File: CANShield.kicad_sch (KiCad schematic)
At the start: 1 part, among them U1 NUCLEO64-F411RE

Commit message: Save schematics
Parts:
- removed U1: NUCLEO64-F411RE, Module:ST_Morpho_Connector_144_STLink, symbol MCU_Module:NUCLEO64-F411RE
- added C1, C2, C3, C4, C5, C6: C, symbol Device:C
- added D1: ESDA5V3L, Package_TO_SOT_SMD:SOT-23-3, symbol Power_Protection:ESDA5V3L
- added FL1: Filter_EMI_LL_1423, symbol Device:Filter_EMI_LL_1423
- added J1, J2: Conn_02x19_Odd_Even, symbol Connector_Generic:Conn_02x19_Odd_Even
- added J3: Conn_01x06_Socket, symbol Connector:Conn_01x06_Socket
- added JP1: SolderJumper_2_Open, symbol Jumper:SolderJumper_2_Open
- added L1, L2, L3, L4: L_Ferrite, symbol Device:L_Ferrite
- added R1, R2, R3: R, symbol Device:R
- added U1: MCP2561-H-MF, Package_DFN_QFN:DFN-8-1EP_3x3mm_P0.65mm_EP1.55x2.4mm, symbol Interface_CAN_LIN:MCP2561-H-MF
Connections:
- new net: J3.3 (Pin_3), L3.1
- new net: C3.1, D1.2 (K), FL1.1, L3.2
- new net: C2.2, R1.2, R2.1, R3.2
- new net: JP1.1 (A), U1.5 (SPLIT)
- new net: JP1.2 (B), R3.1
- new net: C3.2, D1.1 (K), FL1.2, L4.2
- new net: J3.2 (Pin_2), J3.6 (Pin_6), L2.1
- new net: J3.1 (Pin_1), J3.5 (Pin_5), L1.1
- new net: J3.4 (Pin_4), L4.1
- new net +5V: C1.1, U1.3 (VDD)
- new net CAN_H: C4.2, C5.1, FL1.4, R1.1, U1.7 (CANH)
- new net CAN_L: C4.1, C6.2, FL1.3, R2.2, U1.6 (CANL)
- new net CAN_RXD: U1.4 (RXD)
- new net CAN_STBY: U1.8 (STBY)
- new net CAN_TXD: U1.1 (TXD)
- new net GND: C1.2, C2.1, C5.2, C6.1, D1.3 (A), J1.19 (Pin_19), J1.8 (Pin_8), J2.20 (Pin_20), L1.2, U1.2 (VSS), U1.9 (VSS)
- new net VBUS: L2.2

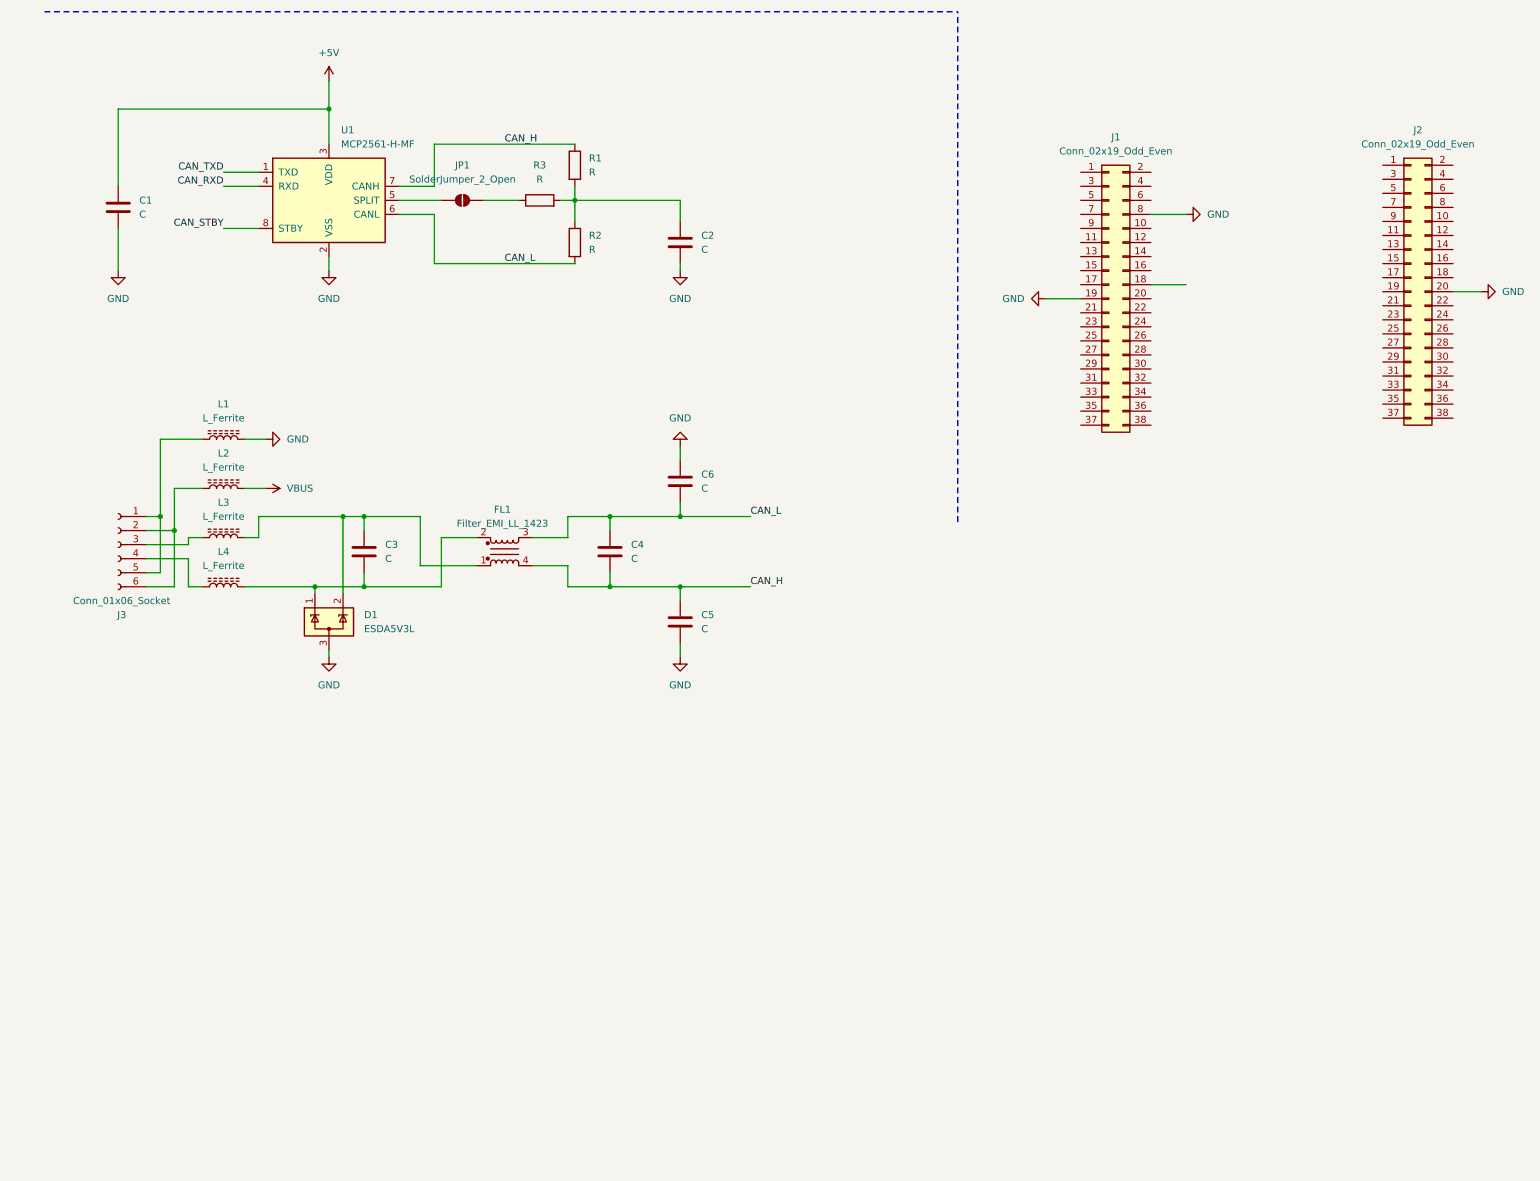
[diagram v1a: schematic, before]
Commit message: Add NXP TJA1443 CAN-FD Chip
Add reference design for CAN-FD chip
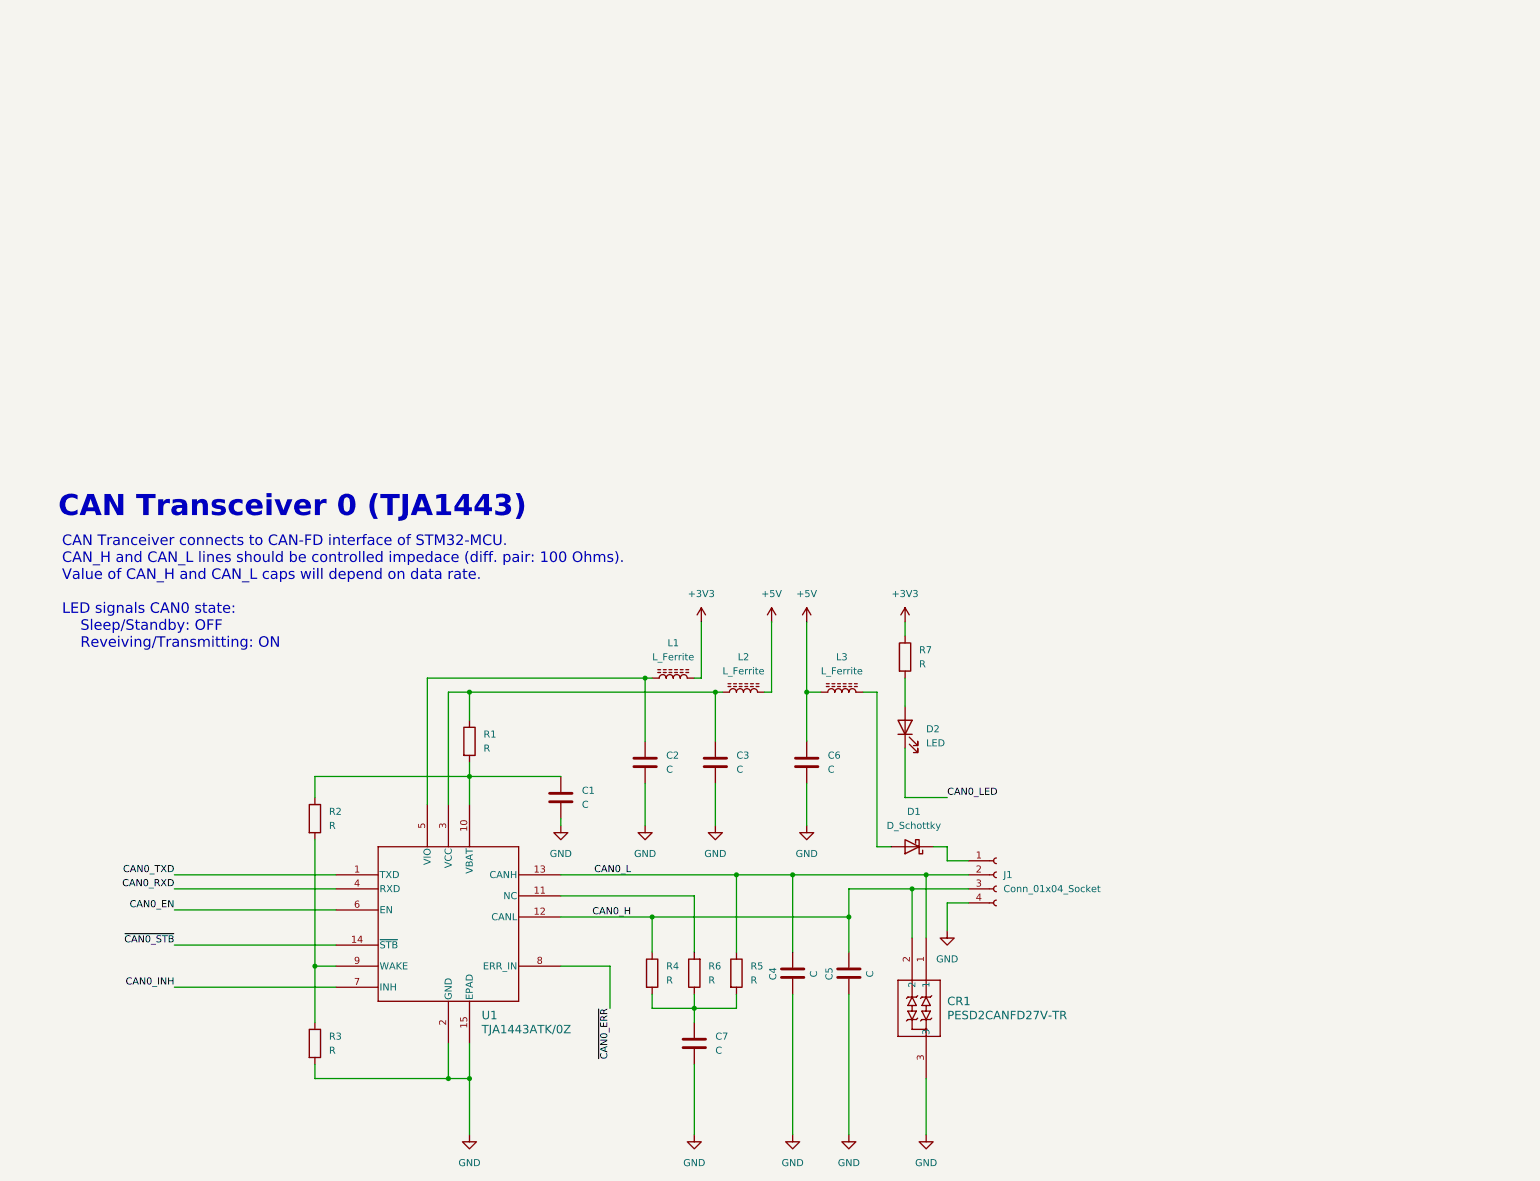
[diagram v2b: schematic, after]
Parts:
- removed D1: ESDA5V3L, Package_TO_SOT_SMD:SOT-23-3, symbol Power_Protection:ESDA5V3L
- removed FL1: Filter_EMI_LL_1423, symbol Device:Filter_EMI_LL_1423
- removed J1, J2: Conn_02x19_Odd_Even, symbol Connector_Generic:Conn_02x19_Odd_Even
- removed J3: Conn_01x06_Socket, symbol Connector:Conn_01x06_Socket
- removed JP1: SolderJumper_2_Open, symbol Jumper:SolderJumper_2_Open
- removed L4: L_Ferrite, symbol Device:L_Ferrite
- removed U1: MCP2561-H-MF, Package_DFN_QFN:DFN-8-1EP_3x3mm_P0.65mm_EP1.55x2.4mm, symbol Interface_CAN_LIN:MCP2561-H-MF
- added C7: C, symbol Device:C
- added CR1: PESD2CANFD27V-TR, SOT23_PESD2_NEX, symbol PESD2CANFD27V:PESD2CANFD27V-TR
- added D1: D_Schottky, symbol Device:D_Schottky
- added D2: LED, symbol Device:LED
- added J1: Conn_01x04_Socket, symbol Connector:Conn_01x04_Socket
- added R4, R5, R6, R7: R, symbol Device:R
- added U1: TJA1443ATK/0Z, HVSON14_SOT1086-2_NXP, symbol TJA1443ATK:TJA1443ATK_0Z
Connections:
- net VBUS is gone; now on net +5V: L2.2
- net +5V: now also C6.1, L3.1; no longer C1.1
- net GND: now also C2.2, C3.2, C4.2, C6.2, R3.2, C7.2, CR1.3, J1.4 (Pin_4), U1.15 (EPAD), U1.2 (GND); no longer C2.1, C6.1, L1.2
- net at C3.1: now also L2.1, R1.1, U1.3 (VCC); no longer L3.2
- net at R1.2, R2.1: now also C1.1, U1.10 (VBAT); no longer C2.2, R3.2
- net at R3.1: now also R2.2, U1.9 (WAKE)
- net at L1.1: now also C2.1, U1.5 (VIO)
- removed net CAN_H: C4.2, C5.1, R1.1
- removed net CAN_L: C4.1, C6.2, R2.2
- new net: R6.2, U1.11 (NC)
- new net: D1.1 (K), J1.1 (Pin_1)
- new net: D1.2 (A), L3.2
- new net: C7.1, R4.2, R5.2, R6.1
- new net: D2.2 (A), R7.2
- new net +3V3: L1.2, R7.1
- new net CAN0_EN: U1.6 (EN)
- new net CAN0_H: C5.1, CR1.2, J1.3 (Pin_3), R4.1, U1.12 (CANL)
- new net CAN0_INH: U1.7 (INH)
- new net CAN0_L: C4.1, CR1.1, J1.2 (Pin_2), R5.1, U1.13 (CANH)
- new net CAN0_LED: D2.1 (K)
- new net CAN0_RXD: U1.4 (RXD)
- new net CAN0_TXD: U1.1 (TXD)
- new net ~{CAN0_ERR}: U1.8 (ERR_IN)
- new net ~{CAN0_STB}: U1.14 (~{STB})
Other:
- note added: "CAN Tranceiver connects to CAN-FD interface of STM32-MCU. CAN_H and CAN_L lines should be controlled impedace (diff. pair: 100 Ohms). Value of CAN_H and CAN_L caps will depend on data rate. LED signals CAN0 state: Sleep/Standby: OFF Reveiving/Transmitting: ON"
- note added: "CAN Transceiver 0 (TJA1443)"
- title: (none) -> CANShield

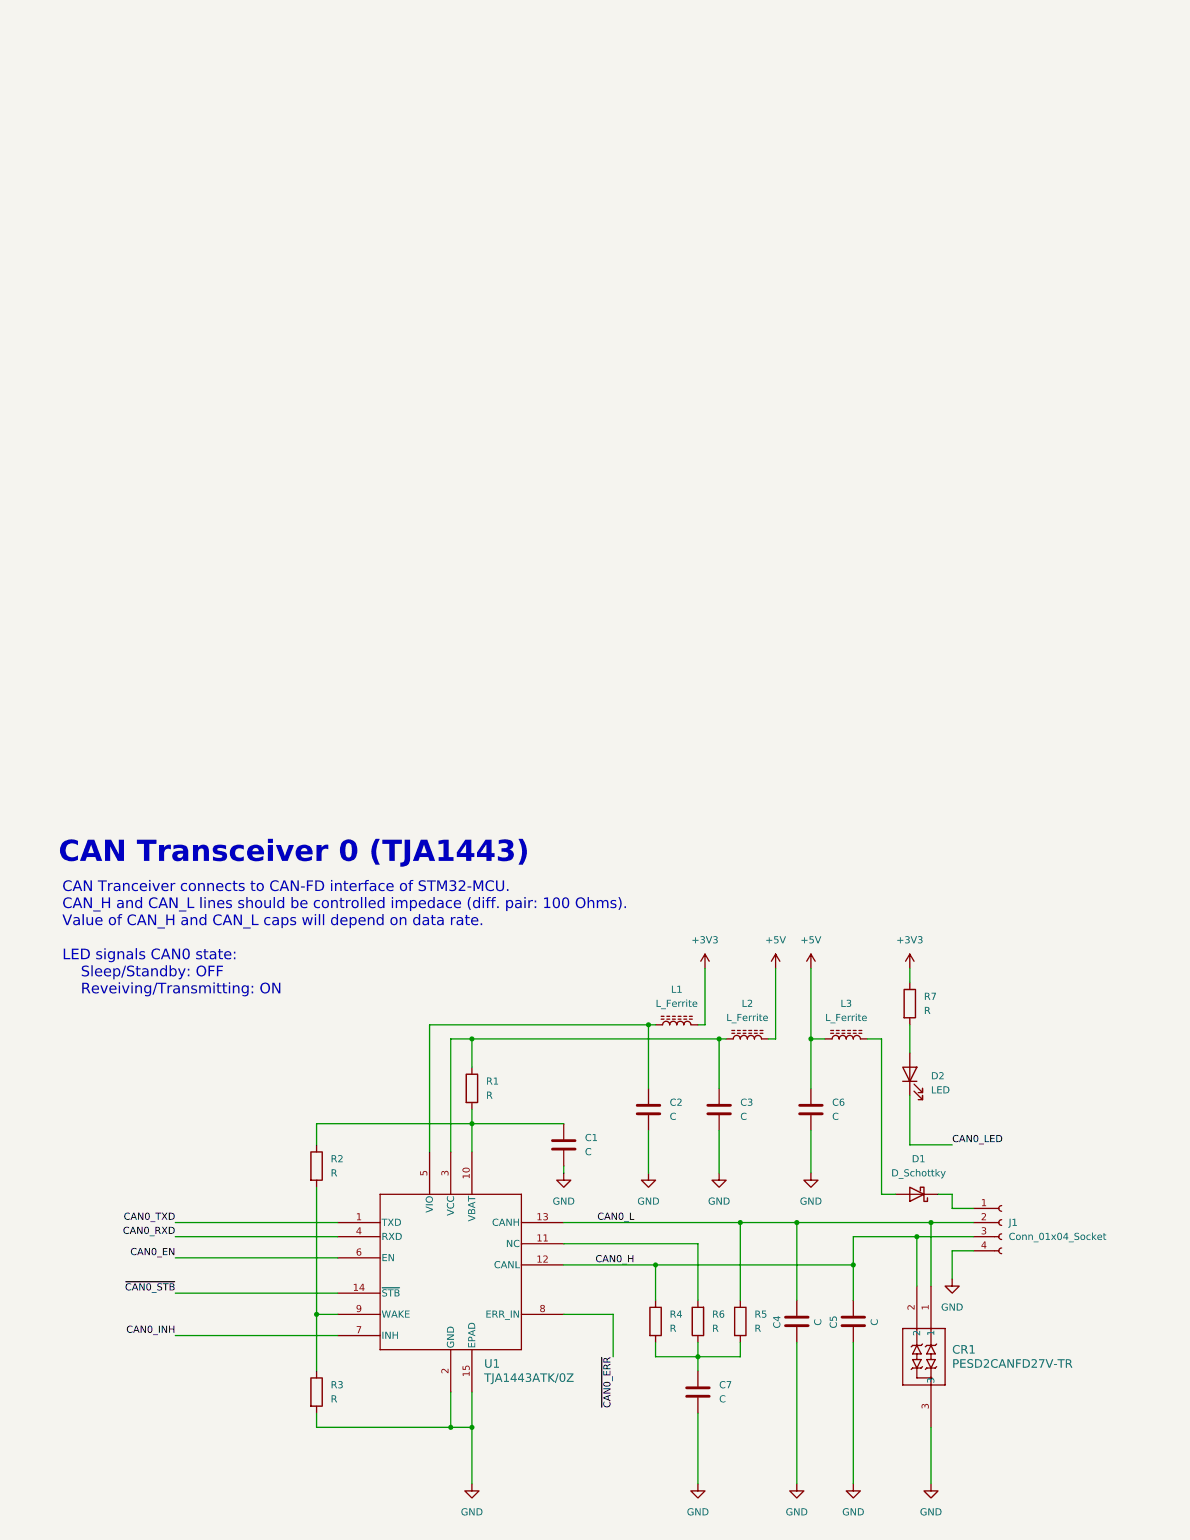
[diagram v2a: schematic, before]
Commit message: Update CANShield.kicad_sch
Add complete Nucleo Pinout
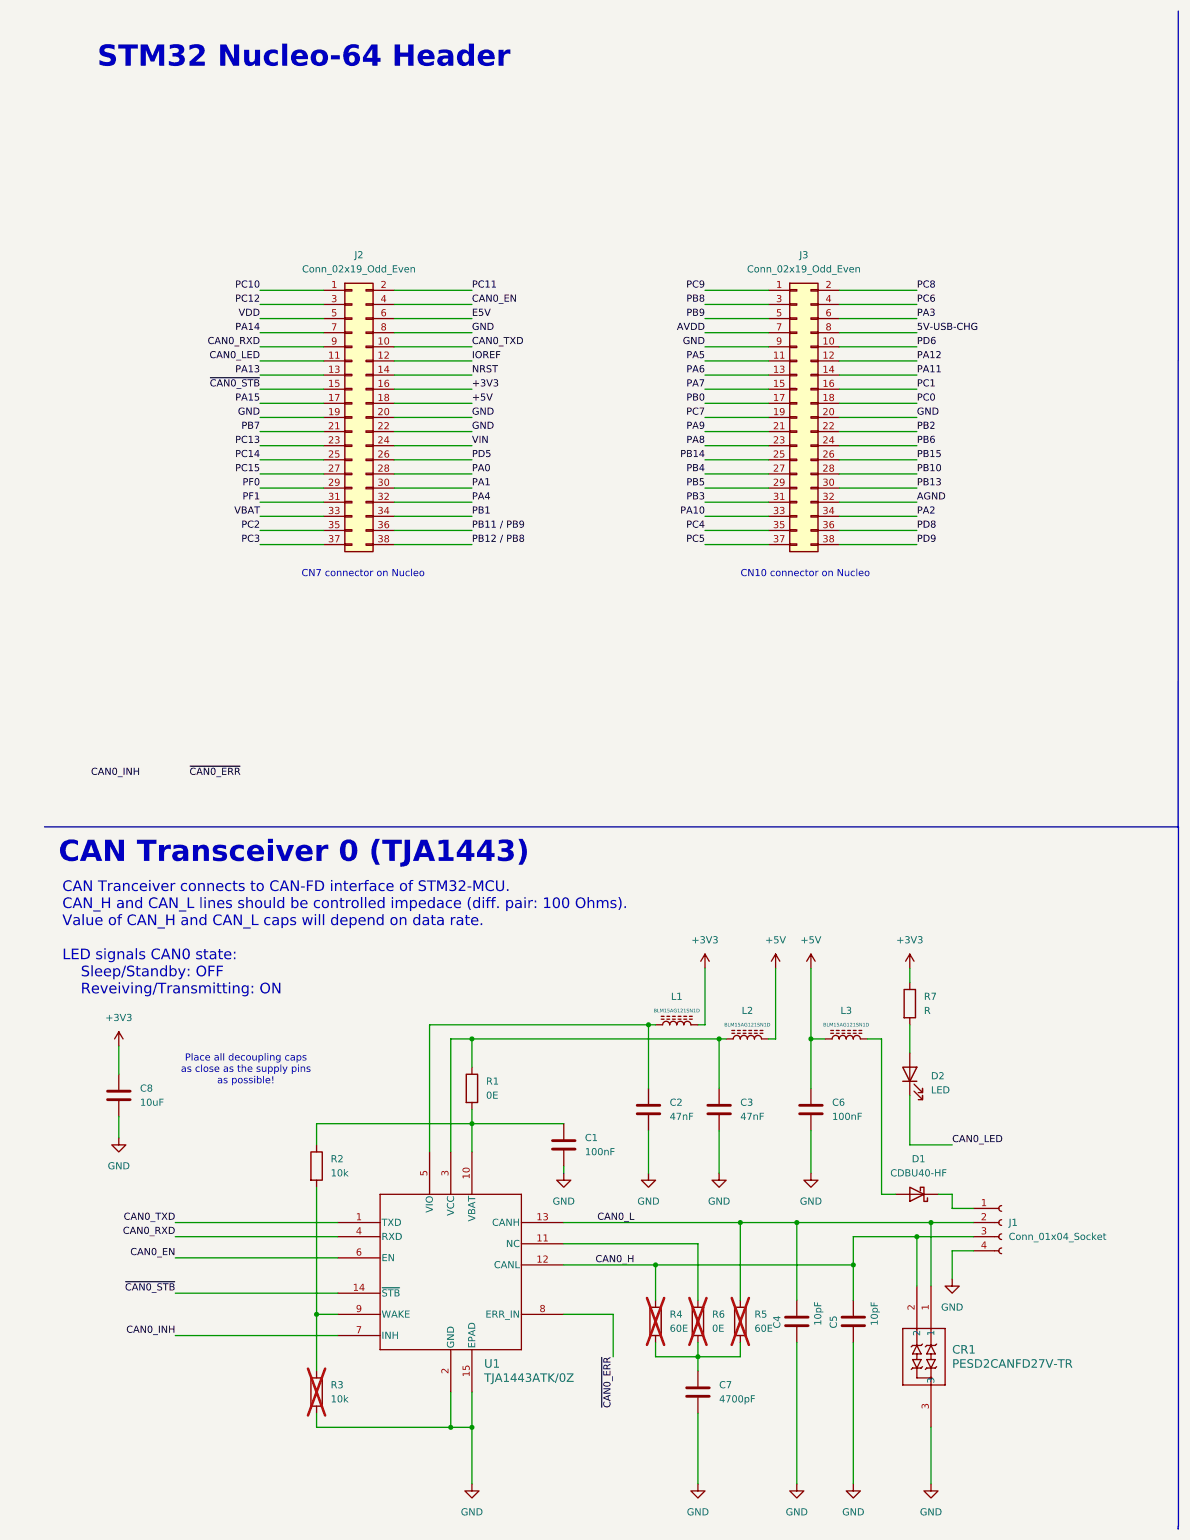
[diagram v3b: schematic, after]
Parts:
- removed D1: D_Schottky, symbol Device:D_Schottky
- added C8: 10uF, symbol Device:C
- added D1: CDBU40-HF, Diode_SMD:D_0603_1608Metric, symbol Diode:CDBU40-HF
- added J2, J3: Conn_02x19_Odd_Even, symbol Connector_Generic:Conn_02x19_Odd_Even
- C1, C6: value C -> 100nF
- C2, C3: value C -> 47nF
- C4, C5: value C -> 10pF
- C7: value C -> 4700pF
- L1, L2, L3: value L_Ferrite -> BLM15AG121SN1D
- R1: value R -> 0E
- R2: value R -> 10k
- R3: value R -> 10k; now not fitted
- R4, R5: value R -> 60E; now not fitted
- R6: value R -> 0E; now not fitted
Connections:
- net +3V3: now also C8.1, J2.16 (Pin_16)
- net +5V: now also J2.18 (Pin_18)
- net CAN0_EN: now also J2.4 (Pin_4)
- net CAN0_LED: now also J2.11 (Pin_11)
- net CAN0_RXD: now also J2.9 (Pin_9)
- net CAN0_TXD: now also J2.10 (Pin_10)
- net GND: now also C8.2, J2.19 (Pin_19), J2.20 (Pin_20), J2.22 (Pin_22), J2.8 (Pin_8), J3.20 (Pin_20), J3.9 (Pin_9)
- net ~{CAN0_STB}: now also J2.15 (Pin_15)
- net at J1.1 (Pin_1): now also D1.1 (K)
- net at L3.2: now also D1.2 (A)
- new net 5V-USB-CHG: J3.8 (Pin_8)
- new net AGND: J3.32 (Pin_32)
- new net AVDD: J3.7 (Pin_7)
- new net E5V: J2.6 (Pin_6)
- new net IOREF: J2.12 (Pin_12)
- new net NRST: J2.14 (Pin_14)
- new net PA0: J2.28 (Pin_28)
- new net PA1: J2.30 (Pin_30)
- new net PA10: J3.33 (Pin_33)
- new net PA11: J3.14 (Pin_14)
- new net PA12: J3.12 (Pin_12)
- new net PA13: J2.13 (Pin_13)
- new net PA14: J2.7 (Pin_7)
- new net PA15: J2.17 (Pin_17)
- new net PA2: J3.34 (Pin_34)
- new net PA3: J3.6 (Pin_6)
- new net PA4: J2.32 (Pin_32)
- new net PA5: J3.11 (Pin_11)
- new net PA6: J3.13 (Pin_13)
- new net PA7: J3.15 (Pin_15)
- new net PA8: J3.23 (Pin_23)
- new net PA9: J3.21 (Pin_21)
- new net PB0: J3.17 (Pin_17)
- new net PB1: J2.34 (Pin_34)
- new net PB10: J3.28 (Pin_28)
- new net PB11 / PB9: J2.36 (Pin_36)
- new net PB12 / PB8: J2.38 (Pin_38)
- new net PB13: J3.30 (Pin_30)
- new net PB14: J3.25 (Pin_25)
- new net PB15: J3.26 (Pin_26)
- new net PB2: J3.22 (Pin_22)
- new net PB3: J3.31 (Pin_31)
- new net PB4: J3.27 (Pin_27)
- new net PB5: J3.29 (Pin_29)
- new net PB6: J3.24 (Pin_24)
- new net PB7: J2.21 (Pin_21)
- new net PB8: J3.3 (Pin_3)
- new net PB9: J3.5 (Pin_5)
- new net PC0: J3.18 (Pin_18)
- new net PC1: J3.16 (Pin_16)
- new net PC10: J2.1 (Pin_1)
- new net PC11: J2.2 (Pin_2)
- new net PC12: J2.3 (Pin_3)
- new net PC13: J2.23 (Pin_23)
- new net PC14: J2.25 (Pin_25)
- new net PC15: J2.27 (Pin_27)
- new net PC2: J2.35 (Pin_35)
- new net PC3: J2.37 (Pin_37)
- new net PC4: J3.35 (Pin_35)
- new net PC5: J3.37 (Pin_37)
- new net PC6: J3.4 (Pin_4)
- new net PC7: J3.19 (Pin_19)
- new net PC8: J3.2 (Pin_2)
- new net PC9: J3.1 (Pin_1)
- new net PD5: J2.26 (Pin_26)
- new net PD6: J3.10 (Pin_10)
- new net PD8: J3.36 (Pin_36)
- new net PD9: J3.38 (Pin_38)
- new net PF0: J2.29 (Pin_29)
- new net PF1: J2.31 (Pin_31)
- new net VBAT: J2.33 (Pin_33)
- new net VDD: J2.5 (Pin_5)
- new net VIN: J2.24 (Pin_24)
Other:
- note added: "CN10 connector on Nucleo"
- note added: "CN7 connector on Nucleo"
- note added: "Place all decoupling caps as close as the supply pins as possible!"
- note added: "STM32 Nucleo-64 Header"
